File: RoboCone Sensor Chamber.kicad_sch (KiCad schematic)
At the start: 13 parts, among them U1 ADS1234IPW

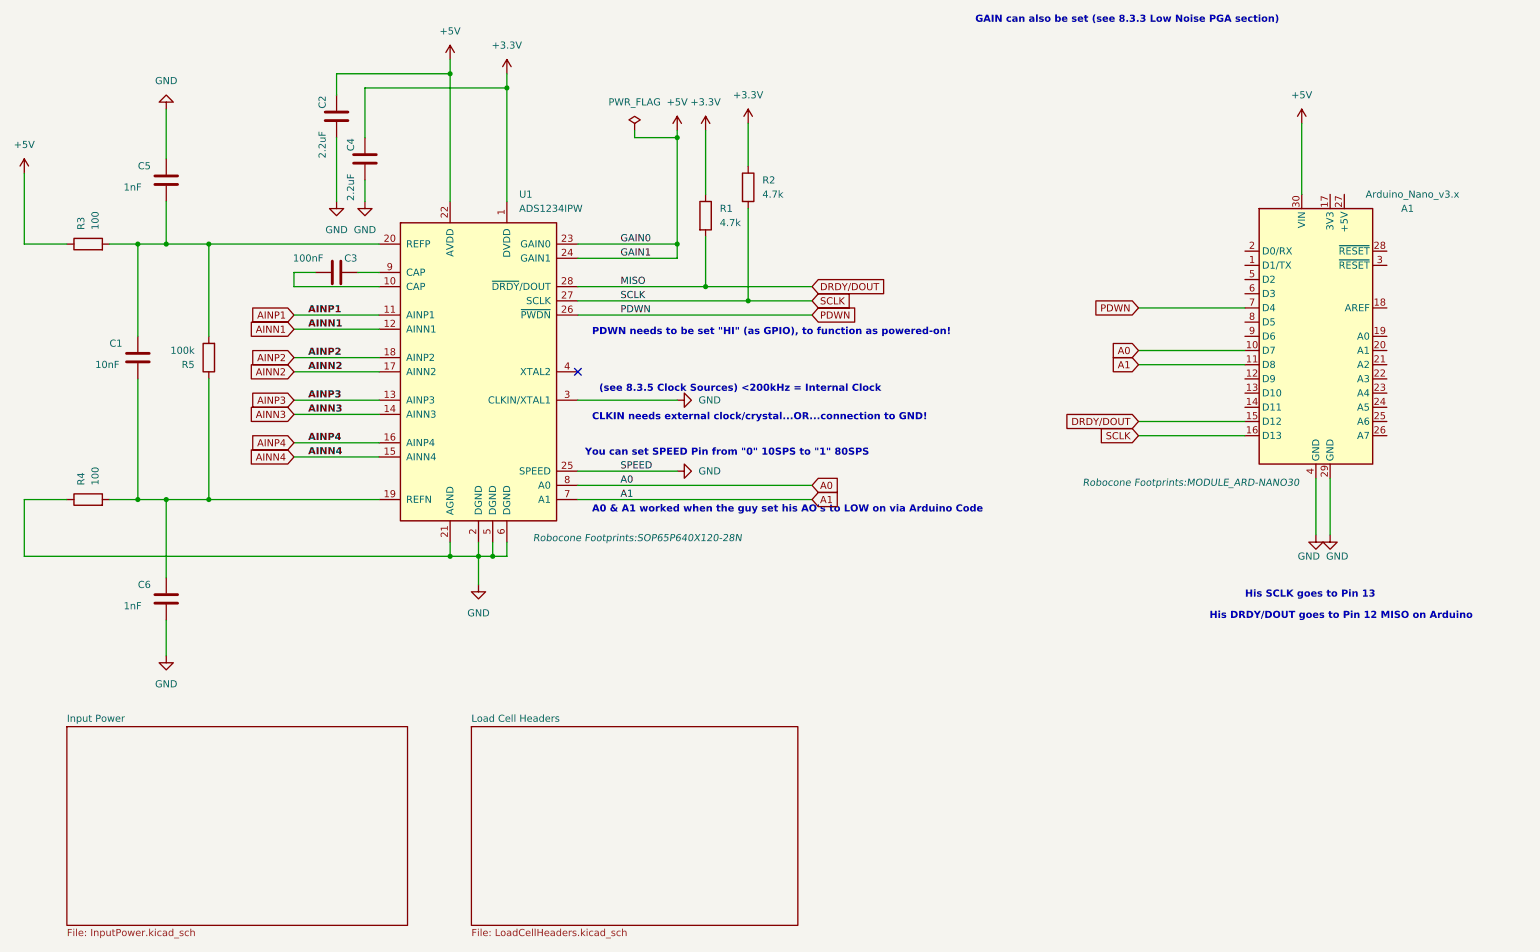
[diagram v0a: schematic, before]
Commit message: Redefined nets - were not setup properly
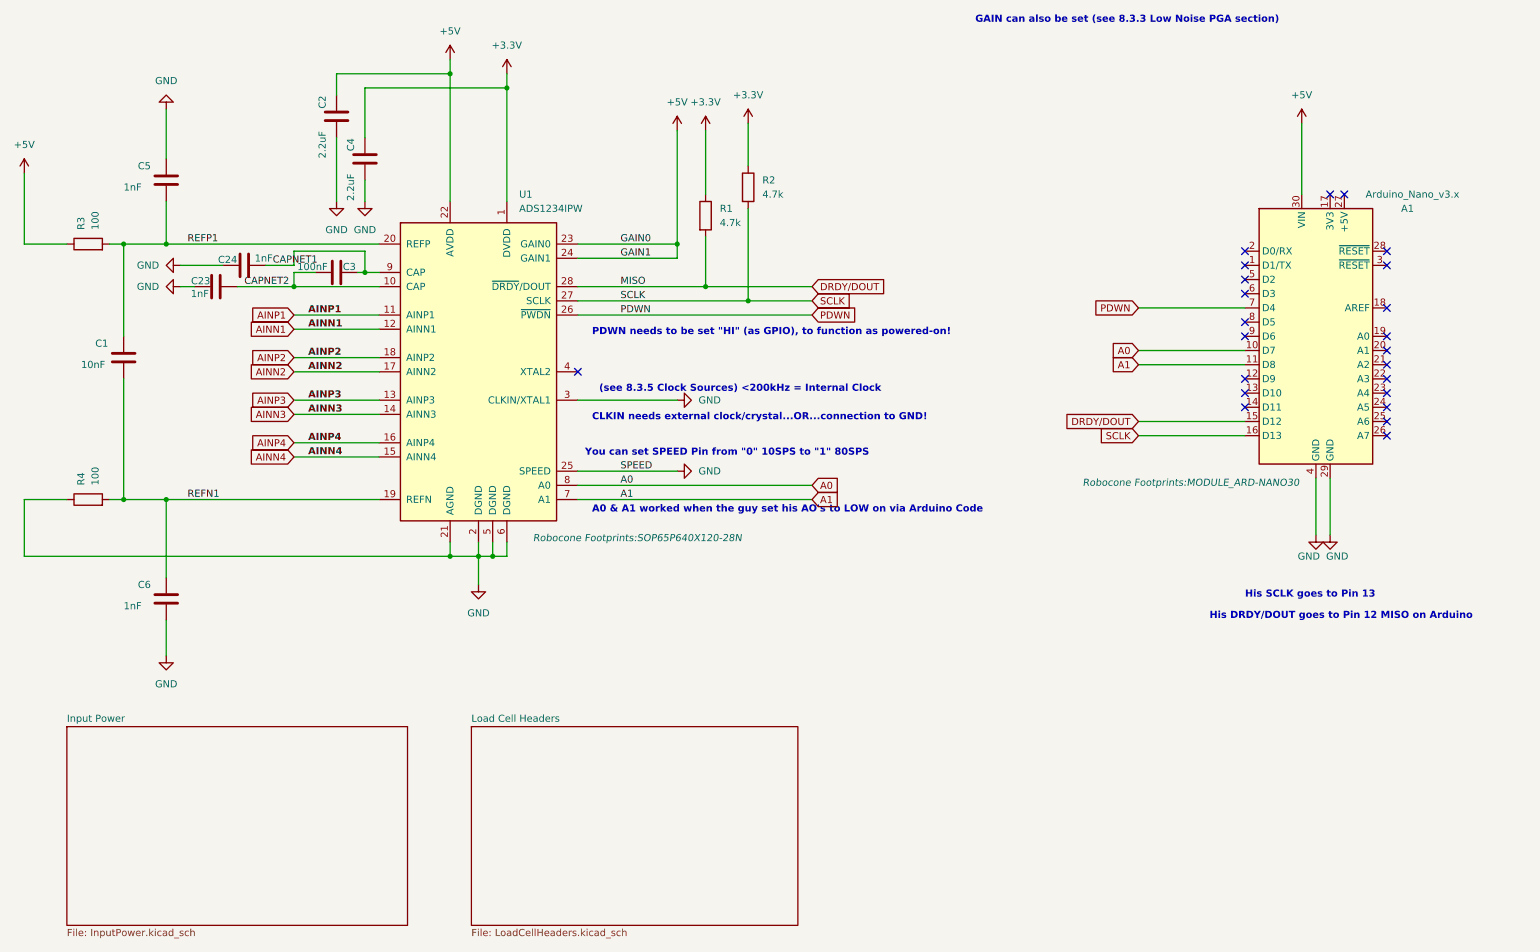
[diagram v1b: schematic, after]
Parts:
- removed R5: 100k, Resistor_SMD:R_0805_2012Metric_Pad1.20x1.40mm_HandSolder, symbol Device:R
- added C23, C24: 1nF, Capacitor_SMD:C_0805_2012Metric_Pad1.18x1.45mm_HandSolder, symbol Device:C
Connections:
- net GND: now also C23.1, C24.1
- net CAPNET2: now reaches C3.1, U1.10 (CAP)
- net CAPNET2: now also C23.2
- net REFN1: now reaches C1.2, C6.1, R4.2, U1.19 (REFN)
- net REFP1: now reaches C1.1, C5.2, R3.2, U1.20 (REFP)
- net CAPNET1: now reaches C3.2, U1.9 (CAP)
- net CAPNET1: now also C24.2
- no-connect marks 1 -> 23
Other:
- moved on the sheet: C1

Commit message: lots of PCB changes
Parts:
- added J7: 691210910002, Robocone Footprints:691210910002, symbol 691210910002:691210910002
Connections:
- net TX1: now reaches A1.1 (D1/TX)
- net TX1: now also J7.1
- net RX1: now reaches A1.2 (D0/RX)
- net RX1: now also J7.2
- no-connect marks 23 -> 21
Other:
- note added: "GAIN0"
- note added: "GAIN1"
- note added: "MISO"
- note added: "SPEED"
